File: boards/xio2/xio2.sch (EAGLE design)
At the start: 269 parts, among them J1 12401598E4#2A, Q1 BSS138, Q2 BSS138, X1 MINI-USB-UX60-MB-5ST, Y2 NX3225SA-12.000MHZ-STD-CSR-1

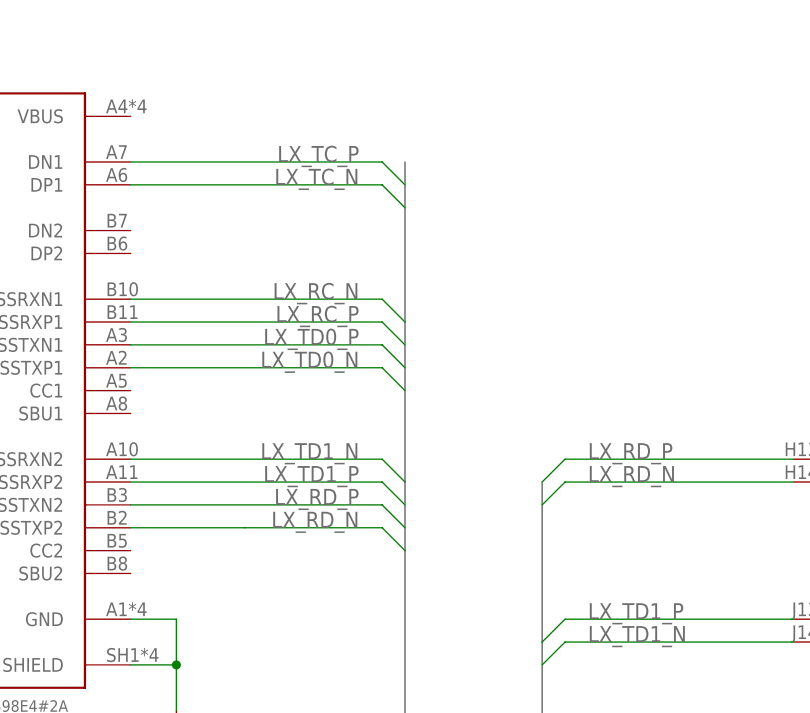
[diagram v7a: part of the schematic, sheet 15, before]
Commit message: Change power resistor/capacitor sizes to prevent overlap of signal wires, given their size for power transmission reasons
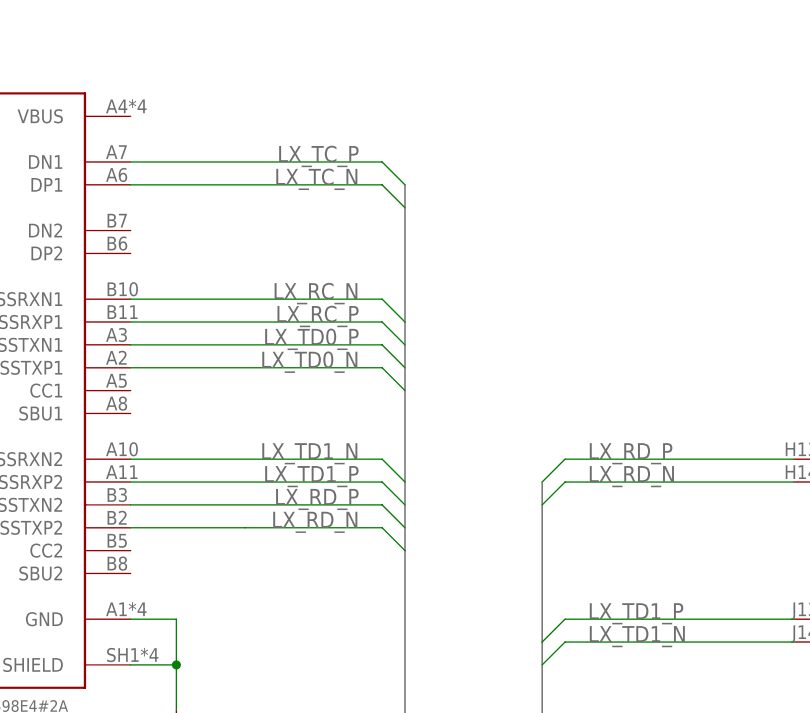
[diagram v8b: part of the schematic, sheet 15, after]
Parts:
- C53, C54, C55, C56, C81: device rcl:C-EUC0201 -> rcl:C-EUC0402
- R58, R59, R61, R62, R63, R64, R65, R83, R84, R85: device rcl:R-EU_R0201 -> rcl:R-EU_R0402
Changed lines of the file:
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@@
 <?xml version="1.0" encoding="utf-8"?>
 <!DOCTYPE eagle SYSTEM "eagle.dtd">
-<eagle version="9.1.0">
+<eagle version="9.1.1">
 <drawing>
 <settings>
@@
 <setting verticaltext="up"/>
 </settings>
-<grid distance="0.1" unitdist="inch" unit="inch" style="lines" multiple="1" display="yes" altdistance="0.01" altunitdist="inch" altunit="inch"/>
+<grid distance="0.1" unitdist="inch" unit="inch" style="lines" multiple="1" display="no" altdistance="0.01" altunitdist="inch" altunit="inch"/>
 <layers>
 <layer number="1" name="Top" color="4" fill="1" visible="yes" active="no"/>
@@
 <part name="P+9" library="supply1" deviceset="+5V" device=""/>
 <part name="P+10" library="supply1" deviceset="+5V" device=""/>
-<part name="R61" library="rcl" library_urn="urn:adsk.eagle:library:334" deviceset="R-EU_" device="R0201" package3d_urn="urn:adsk.eagle:package:23593/1" value="10K"/>
-<part name="R62" library="rcl" library_urn="urn:adsk.eagle:library:334" deviceset="R-EU_" device="R0201" package3d_urn="urn:adsk.eagle:package:23593/1" value="10K"/>
-<part name="R63" library="rcl" library_urn="urn:adsk.eagle:library:334" deviceset="R-EU_" device="R0201" package3d_urn="urn:adsk.eagle:package:23593/1" value="10K"/>
-<part name="R64" library="rcl" library_urn="urn:adsk.eagle:library:334" deviceset="R-EU_" device="R0201" package3d_urn="urn:adsk.eagle:package:23593/1" value="10K"/>
-<part name="R65" library="rcl" library_urn="urn:adsk.eagle:library:334" deviceset="R-EU_" device="R0201" package3d_urn="urn:adsk.eagle:package:23593/1" value="10K"/>
+<part name="R61" library="rcl" library_urn="urn:adsk.eagle:library:334" deviceset="R-EU_" device="R0402" package3d_urn="urn:adsk.eagle:package:23547/2" value="10K"/>
+<part name="R62" library="rcl" library_urn="urn:adsk.eagle:library:334" deviceset="R-EU_" device="R0402" package3d_urn="urn:adsk.eagle:package:23547/2" value="10K"/>
+<part name="R63" library="rcl" library_urn="urn:adsk.eagle:library:334" deviceset="R-EU_" device="R0402" package3d_urn="urn:adsk.eagle:package:23547/2" value="10K"/>
+<part name="R64" library="rcl" library_urn="urn:adsk.eagle:library:334" deviceset="R-EU_" device="R0402" package3d_urn="urn:adsk.eagle:package:23547/2" value="10K"/>
+<part name="R65" library="rcl" library_urn="urn:adsk.eagle:library:334" deviceset="R-EU_" device="R0402" package3d_urn="urn:adsk.eagle:package:23547/2" value="10K"/>
 <part name="FRAME3" library="frames" library_urn="urn:adsk.eagle:library:229" deviceset="A3L-LOC" device=""/>
 <part name="FRAME4" library="frames" library_urn="urn:adsk.eagle:library:229" deviceset="A3L-LOC" device=""/>
@@
 <part name="R27" library="rcl" library_urn="urn:adsk.eagle:library:334" deviceset="R-EU_" device="R0201" package3d_urn="urn:adsk.eagle:package:23593/1" value="33R"/>
 <part name="+3V30" library="supply1" library_urn="urn:adsk.eagle:library:371" deviceset="+3V3" device=""/>
-<part name="C53" library="rcl" library_urn="urn:adsk.eagle:library:334" deviceset="C-EU" device="C0201" package3d_urn="urn:adsk.eagle:package:23690/2" value="0.1uF"/>
+<part name="C53" library="rcl" library_urn="urn:adsk.eagle:library:334" deviceset="C-EU" device="C0402" package3d_urn="urn:adsk.eagle:package:23626/1" value="0.1uF"/>
 <part name="SUPPLY8" library="supply2" deviceset="GND" device=""/>
-<part name="C54" library="rcl" library_urn="urn:adsk.eagle:library:334" deviceset="C-EU" device="C0201" package3d_urn="urn:adsk.eagle:package:23690/2" value="0.1uF"/>
+<part name="C54" library="rcl" library_urn="urn:adsk.eagle:library:334" deviceset="C-EU" device="C0402" package3d_urn="urn:adsk.eagle:package:23626/1" value="0.1uF"/>
 <part name="SUPPLY20" library="supply2" deviceset="GND" device=""/>
 <part name="SUPPLY21" library="supply2" deviceset="GND" device=""/>
-<part name="C55" library="rcl" library_urn="urn:adsk.eagle:library:334" deviceset="C-EU" device="C0201" package3d_urn="urn:adsk.eagle:package:23690/2" value="0.1uF"/>
+<part name="C55" library="rcl" library_urn="urn:adsk.eagle:library:334" deviceset="C-EU" device="C0402" package3d_urn="urn:adsk.eagle:package:23626/1" value="0.1uF"/>
 <part name="SUPPLY47" library="supply2" deviceset="GND" device=""/>
-<part name="C56" library="rcl" library_urn="urn:adsk.eagle:library:334" deviceset="C-EU" device="C0201" package3d_urn="urn:adsk.eagle:package:23690/2" value="0.1uF"/>
+<part name="C56" library="rcl" library_urn="urn:adsk.eagle:library:334" deviceset="C-EU" device="C0402" package3d_urn="urn:adsk.eagle:package:23626/1" value="0.1uF"/>
 <part name="SUPPLY22" library="supply2" deviceset="GND" device=""/>
-<part name="C81" library="rcl" library_urn="urn:adsk.eagle:library:334" deviceset="C-EU" device="C0201" package3d_urn="urn:adsk.eagle:package:23690/2" value="0.1uF"/>
+<part name="C81" library="rcl" library_urn="urn:adsk.eagle:library:334" deviceset="C-EU" device="C0402" package3d_urn="urn:adsk.eagle:package:23626/1" value="0.1uF"/>
 <part name="C134" library="rcl" library_urn="urn:adsk.eagle:library:334" deviceset="C-EU" device="C0201" package3d_urn="urn:adsk.eagle:package:23690/2" value="0.1uF"/>
 <part name="R53" library="rcl" library_urn="urn:adsk.eagle:library:334" deviceset="R-EU_" device="R0201" package3d_urn="urn:adsk.eagle:package:23593/1" value="0R"/>
 <part name="R56" library="rcl" library_urn="urn:adsk.eagle:library:334" deviceset="R-EU_" device="R0201" package3d_urn="urn:adsk.eagle:package:23593/1" value="0R"/>
-<part name="R58" library="rcl" library_urn="urn:adsk.eagle:library:334" deviceset="R-EU_" device="R0201" package3d_urn="urn:adsk.eagle:package:23593/1" value="0R"/>
-<part name="R59" library="rcl" library_urn="urn:adsk.eagle:library:334" deviceset="R-EU_" device="R0201" package3d_urn="urn:adsk.eagle:package:23593/1" value="0R"/>
-<part name="R83" library="rcl" library_urn="urn:adsk.eagle:library:334" deviceset="R-EU_" device="R0201" package3d_urn="urn:adsk.eagle:package:23593/1" value="0R"/>
-<part name="R84" library="rcl" library_urn="urn:adsk.eagle:library:334" deviceset="R-EU_" device="R0201" package3d_urn="urn:adsk.eagle:package:23593/1" value="0R"/>
-<part name="R85" library="rcl" library_urn="urn:adsk.eagle:library:334" deviceset="R-EU_" device="R0201" package3d_urn="urn:adsk.eagle:package:23593/1" value="0R"/>
+<part name="R58" library="rcl" library_urn="urn:adsk.eagle:library:334" deviceset="R-EU_" device="R0402" package3d_urn="urn:adsk.eagle:package:23547/2" value="0R"/>
+<part name="R59" library="rcl" library_urn="urn:adsk.eagle:library:334" deviceset="R-EU_" device="R0402" package3d_urn="urn:adsk.eagle:package:23547/2" value="0R"/>
+<part name="R83" library="rcl" library_urn="urn:adsk.eagle:library:334" deviceset="R-EU_" device="R0402" package3d_urn="urn:adsk.eagle:package:23547/2" value="0R"/>
+<part name="R84" library="rcl" library_urn="urn:adsk.eagle:library:334" deviceset="R-EU_" device="R0402" package3d_urn="urn:adsk.eagle:package:23547/2" value="0R"/>
+<part name="R85" library="rcl" library_urn="urn:adsk.eagle:library:334" deviceset="R-EU_" device="R0402" package3d_urn="urn:adsk.eagle:package:23547/2" value="0R"/>
 <part name="R89" library="rcl" library_urn="urn:adsk.eagle:library:334" deviceset="R-EU_" device="R0201" package3d_urn="urn:adsk.eagle:package:23593/1" value="10K"/>
 <part name="R90" library="rcl" library_urn="urn:adsk.eagle:library:334" deviceset="R-EU_" device="R0201" package3d_urn="urn:adsk.eagle:package:23593/1" value="10K"/>
@@
 <bus name="LX_LINK:LX_RC_N,LX_RC_P,LX_RD_N,LX_RD_P,LX_TC_N,LX_TC_P,LX_TD0_N,LX_TD0_P,LX_TD1_N,LX_TD1_P">
 <segment>
-<wire x1="-104.14" y1="35.56" x2="-104.14" y2="-7.62" width="0.762" layer="92"/>
+<wire x1="-104.14" y1="33.02" x2="-104.14" y2="-7.62" width="0.762" layer="92"/>
 </segment>
 <segment>
